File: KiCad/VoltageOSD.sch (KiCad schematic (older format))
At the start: 19 parts, among them J1 Camera, J2 VTX, J3 RST, J4 MISO, J5 SCK, U1 LMH1980, U2 ATTINY13A-MMU

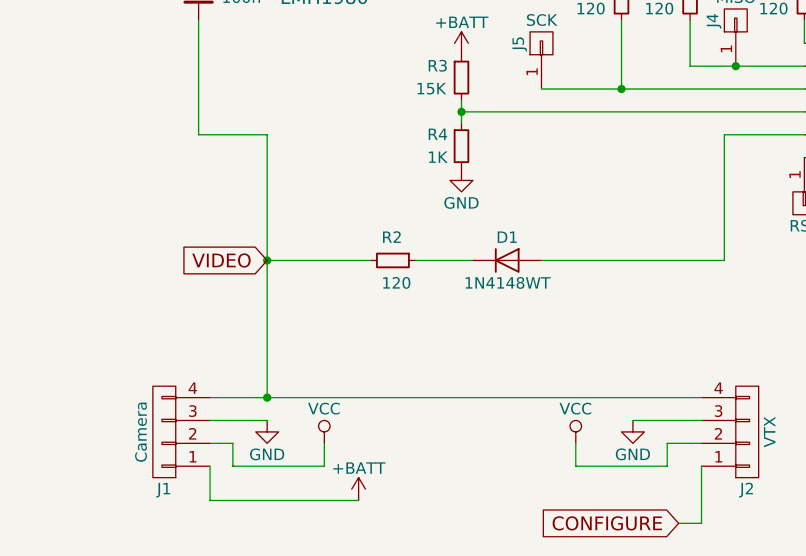
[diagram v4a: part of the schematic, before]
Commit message: Adjusted schematic and PCB (not critical values)
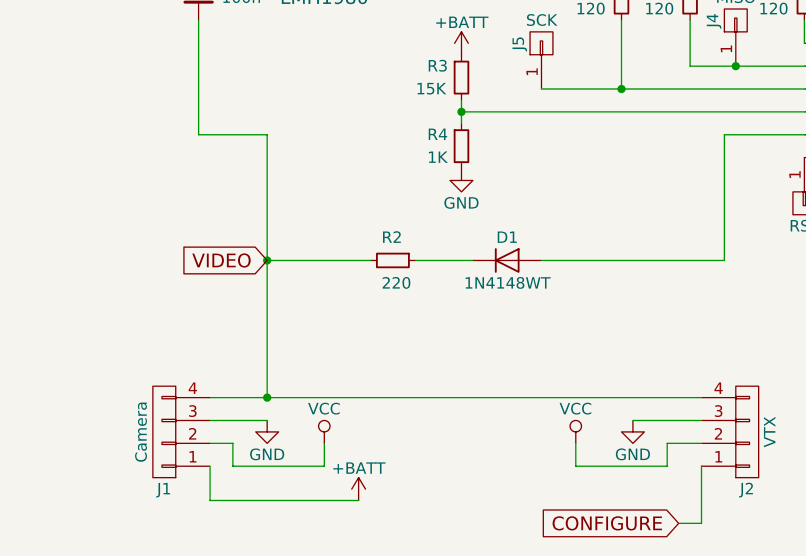
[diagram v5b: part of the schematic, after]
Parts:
- R2: value 120 -> 220
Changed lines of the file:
@@
 P 2900 4400
 F 0 "R2" V 2800 4350 50  0000 L CNN
-F 1 "120" V 3000 4350 50  0000 L CNN
+F 1 "220" V 3000 4350 50  0000 L CNN
 F 2 "Resistors_SMD:R_0402_NoSilk" H 2900 4400 50  0001 C CNN
 F 3 "" H 2900 4400 50  0001 C CNN
